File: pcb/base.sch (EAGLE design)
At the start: 13 parts, among them IC1 TINY24/44/84-PU, J1 22-27-2051-05, J2 22-27-2051-05, J3 22-27-2051-05, J4 22-27-2051-05, J5 22-27-2051-05, J6 22-27-2021-02

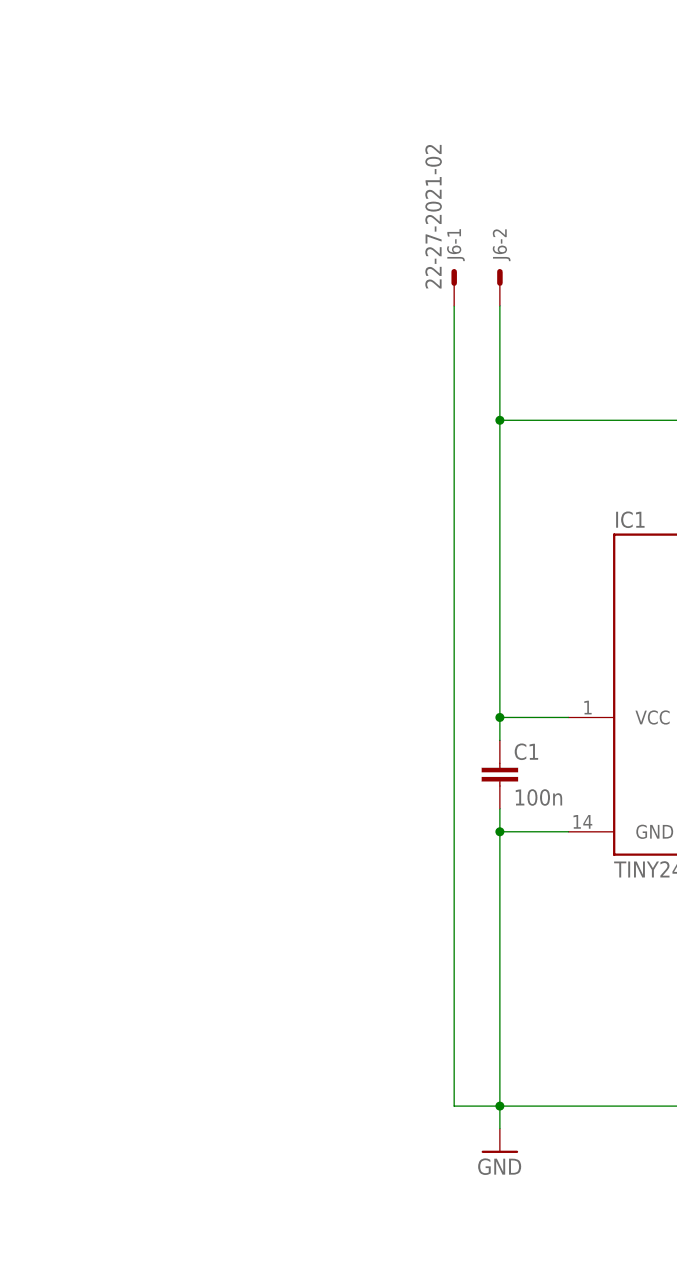
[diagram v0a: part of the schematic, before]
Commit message: add voltage regulator and other clamp
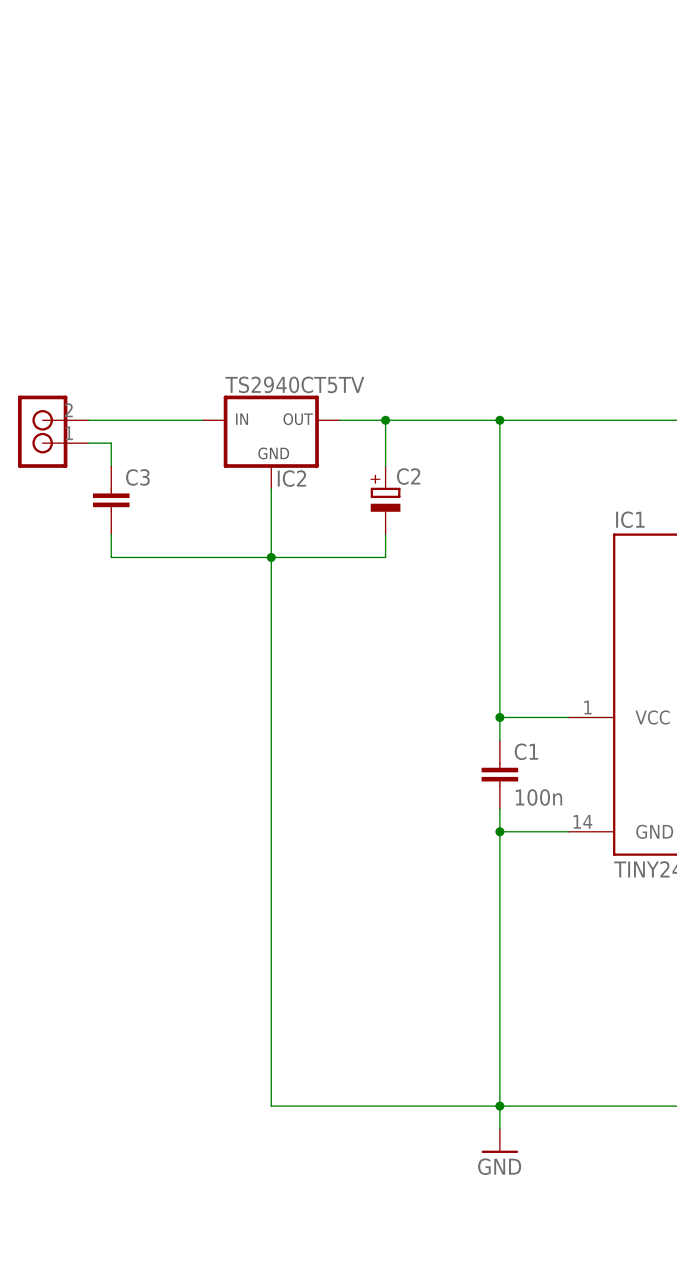
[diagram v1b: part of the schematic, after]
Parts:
- removed J6: 22-27-2021-02, con-molex:22-27-2021-02
- added C2: (no value), rcl:CPOL-EUE2.5-7
- added C3: (no value), rcl:C-EU025-025X050
- added IC2: TS2940CT5TV, n39:TS2940CT5TV
- added U$9: RIACON_101_2, n39:RIACON_101_2
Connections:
- new net N$4: IC2.IN, U$9.2
- new net N$6: C3.1, U$9.1
- net GND: now also C2.-, C3.2, IC2.GND; no longer J6-1.S
- net VCC: now also C2.+, IC2.OUT; no longer J6-2.S
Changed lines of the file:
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@@
 <part name="R3" library="pot" deviceset="TRIM_EU-" device="CIP20C-6MM" value="100k"/>
 <part name="R4" library="pot" deviceset="TRIM_EU-" device="CIP20C-6MM" value="100k"/>
-<part name="J6" library="con-molex" deviceset="22-?-02" device="27-2021"/>
+<part name="U$9" library="n39" deviceset="RIACON_101_2" device=""/>
+<part name="IC2" library="n39" deviceset="TS2940" device="TV" technology="CT5"/>
+<part name="C2" library="rcl" deviceset="CPOL-EU" device="E2.5-7"/>
+<part name="C3" library="rcl" deviceset="C-EU" device="025-025X050"/>
 </parts>
 <sheets>
@@
 <instance part="R3" gate="1" x="129.54" y="43.18" rot="R180"/>
 <instance part="R4" gate="1" x="119.38" y="33.02" rot="R180"/>
-<instance part="J6" gate="-1" x="7.62" y="91.44" rot="R90"/>
-<instance part="J6" gate="-2" x="12.7" y="91.44" rot="R90"/>
+<instance part="U$9" gate="G$1" x="-38.1" y="73.66" rot="R180"/>
+<instance part="IC2" gate="IC$1" x="-12.7" y="76.2"/>
+<instance part="C2" gate="G$1" x="0" y="68.58"/>
+<instance part="C3" gate="G$1" x="-30.48" y="68.58"/>
 </instances>
 <busses>
@@
 <pinref part="P+1" gate="VCC" pin="VCC"/>
 <wire x1="96.52" y1="88.9" x2="96.52" y2="76.2" width="0.1524" layer="91"/>
-<pinref part="J6" gate="-2" pin="S"/>
-<wire x1="12.7" y1="88.9" x2="12.7" y2="76.2" width="0.1524" layer="91"/>
+<pinref part="IC2" gate="IC$1" pin="OUT"/>
+<pinref part="C2" gate="G$1" pin="+"/>
+<wire x1="-5.08" y1="76.2" x2="0" y2="76.2" width="0.1524" layer="91"/>
+<wire x1="0" y1="71.12" x2="0" y2="76.2" width="0.1524" layer="91"/>
+<wire x1="0" y1="76.2" x2="12.7" y2="76.2" width="0.1524" layer="91"/>
+<junction x="0" y="76.2"/>
 <junction x="12.7" y="76.2"/>
 </segment>
@@
 <junction x="154.94" y="81.28"/>
 <junction x="12.7" y="0"/>
-<pinref part="J6" gate="-1" pin="S"/>
-<wire x1="7.62" y1="88.9" x2="7.62" y2="0" width="0.1524" layer="91"/>
-<wire x1="7.62" y1="0" x2="12.7" y2="0" width="0.1524" layer="91"/>
+<pinref part="IC2" gate="IC$1" pin="GND"/>
+<wire x1="12.7" y1="0" x2="-12.7" y2="0" width="0.1524" layer="91"/>
+<wire x1="-12.7" y1="0" x2="-12.7" y2="60.96" width="0.1524" layer="91"/>
+<pinref part="C3" gate="G$1" pin="2"/>
+<wire x1="-12.7" y1="60.96" x2="-12.7" y2="68.58" width="0.1524" layer="91"/>
+<wire x1="-30.48" y1="63.5" x2="-30.48" y2="60.96" width="0.1524" layer="91"/>
+<wire x1="-30.48" y1="60.96" x2="-12.7" y2="60.96" width="0.1524" layer="91"/>
+<pinref part="C2" gate="G$1" pin="-"/>
+<wire x1="0" y1="63.5" x2="0" y2="60.96" width="0.1524" layer="91"/>
+<wire x1="0" y1="60.96" x2="-12.7" y2="60.96" width="0.1524" layer="91"/>
+<junction x="-12.7" y="60.96"/>
 </segment>
 <segment>
@@
 </segment>
 </net>
+<net name="N$4" class="0">
+<segment>
+<pinref part="U$9" gate="G$1" pin="2"/>
+<pinref part="IC2" gate="IC$1" pin="IN"/>
+<wire x1="-33.02" y1="76.2" x2="-20.32" y2="76.2" width="0.1524" layer="91"/>
+</segment>
+</net>
+<net name="N$6" class="0">
+<segment>
+<pinref part="U$9" gate="G$1" pin="1"/>
+<pinref part="C3" gate="G$1" pin="1"/>
+<wire x1="-33.02" y1="73.66" x2="-30.48" y2="73.66" width="0.1524" layer="91"/>
+<wire x1="-30.48" y1="73.66" x2="-30.48" y2="71.12" width="0.1524" layer="91"/>
+</segment>
+</net>

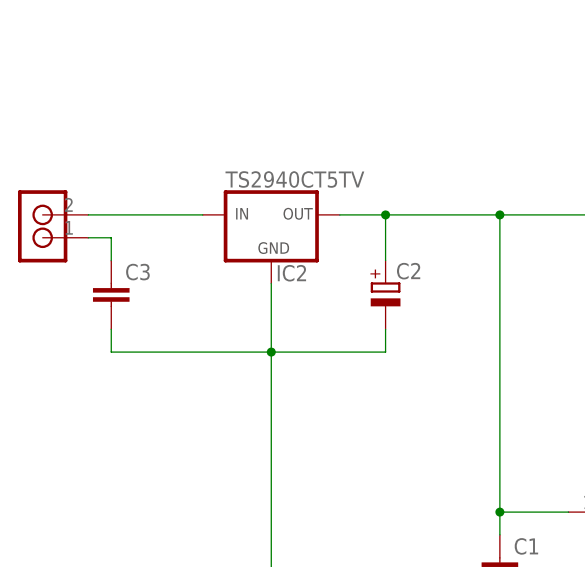
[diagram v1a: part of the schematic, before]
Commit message: route voltage regulator
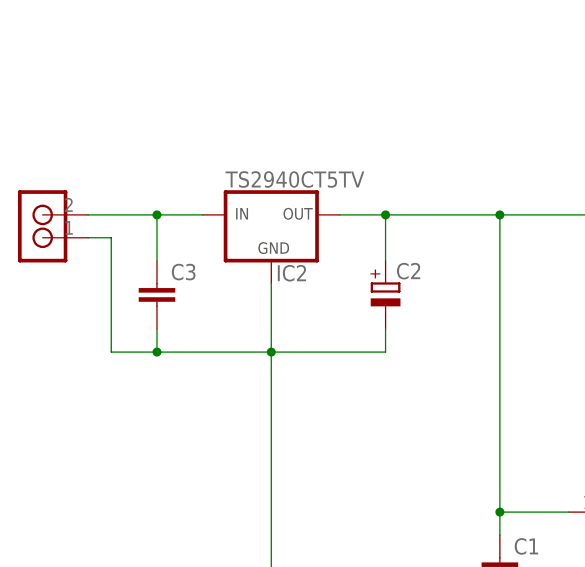
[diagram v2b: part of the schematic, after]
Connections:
- removed net N$6: C3.1, U$9.1
- net GND: now also U$9.1
- net N$4: now also C3.1
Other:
- moved on the sheet: C3
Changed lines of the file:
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@@
 <instance part="IC2" gate="IC$1" x="-12.7" y="76.2"/>
 <instance part="C2" gate="G$1" x="0" y="68.58"/>
-<instance part="C3" gate="G$1" x="-30.48" y="68.58"/>
+<instance part="C3" gate="G$1" x="-25.4" y="68.58"/>
 </instances>
 <busses>
@@
 <pinref part="C3" gate="G$1" pin="2"/>
 <wire x1="-12.7" y1="60.96" x2="-12.7" y2="68.58" width="0.1524" layer="91"/>
-<wire x1="-30.48" y1="63.5" x2="-30.48" y2="60.96" width="0.1524" layer="91"/>
-<wire x1="-30.48" y1="60.96" x2="-12.7" y2="60.96" width="0.1524" layer="91"/>
+<wire x1="-25.4" y1="63.5" x2="-25.4" y2="60.96" width="0.1524" layer="91"/>
+<wire x1="-25.4" y1="60.96" x2="-12.7" y2="60.96" width="0.1524" layer="91"/>
 <pinref part="C2" gate="G$1" pin="-"/>
 <wire x1="0" y1="63.5" x2="0" y2="60.96" width="0.1524" layer="91"/>
 <wire x1="0" y1="60.96" x2="-12.7" y2="60.96" width="0.1524" layer="91"/>
 <junction x="-12.7" y="60.96"/>
+<pinref part="U$9" gate="G$1" pin="1"/>
+<wire x1="-33.02" y1="73.66" x2="-30.48" y2="73.66" width="0.1524" layer="91"/>
+<wire x1="-30.48" y1="73.66" x2="-30.48" y2="60.96" width="0.1524" layer="91"/>
+<wire x1="-30.48" y1="60.96" x2="-25.4" y2="60.96" width="0.1524" layer="91"/>
+<junction x="-25.4" y="60.96"/>
 </segment>
 <segment>
@@
 <pinref part="U$9" gate="G$1" pin="2"/>
 <pinref part="IC2" gate="IC$1" pin="IN"/>
-<wire x1="-33.02" y1="76.2" x2="-20.32" y2="76.2" width="0.1524" layer="91"/>
-</segment>
-</net>
-<net name="N$6" class="0">
-<segment>
-<pinref part="U$9" gate="G$1" pin="1"/>
+<wire x1="-33.02" y1="76.2" x2="-25.4" y2="76.2" width="0.1524" layer="91"/>
 <pinref part="C3" gate="G$1" pin="1"/>
-<wire x1="-33.02" y1="73.66" x2="-30.48" y2="73.66" width="0.1524" layer="91"/>
-<wire x1="-30.48" y1="73.66" x2="-30.48" y2="71.12" width="0.1524" layer="91"/>
-</segment>
-</net>
+<wire x1="-25.4" y1="76.2" x2="-20.32" y2="76.2" width="0.1524" layer="91"/>
+<wire x1="-25.4" y1="71.12" x2="-25.4" y2="76.2" width="0.1524" layer="91"/>
+<junction x="-25.4" y="76.2"/>
+</segment>
+</net>
